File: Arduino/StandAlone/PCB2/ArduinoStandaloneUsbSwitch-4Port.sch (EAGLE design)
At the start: 66 parts, among them U1 INA219AIDCNRSOIC, U2 LM3526M-L, U3 LM3526M-L, U4 ARDUINO_MKRFOX1200PROTOPADS

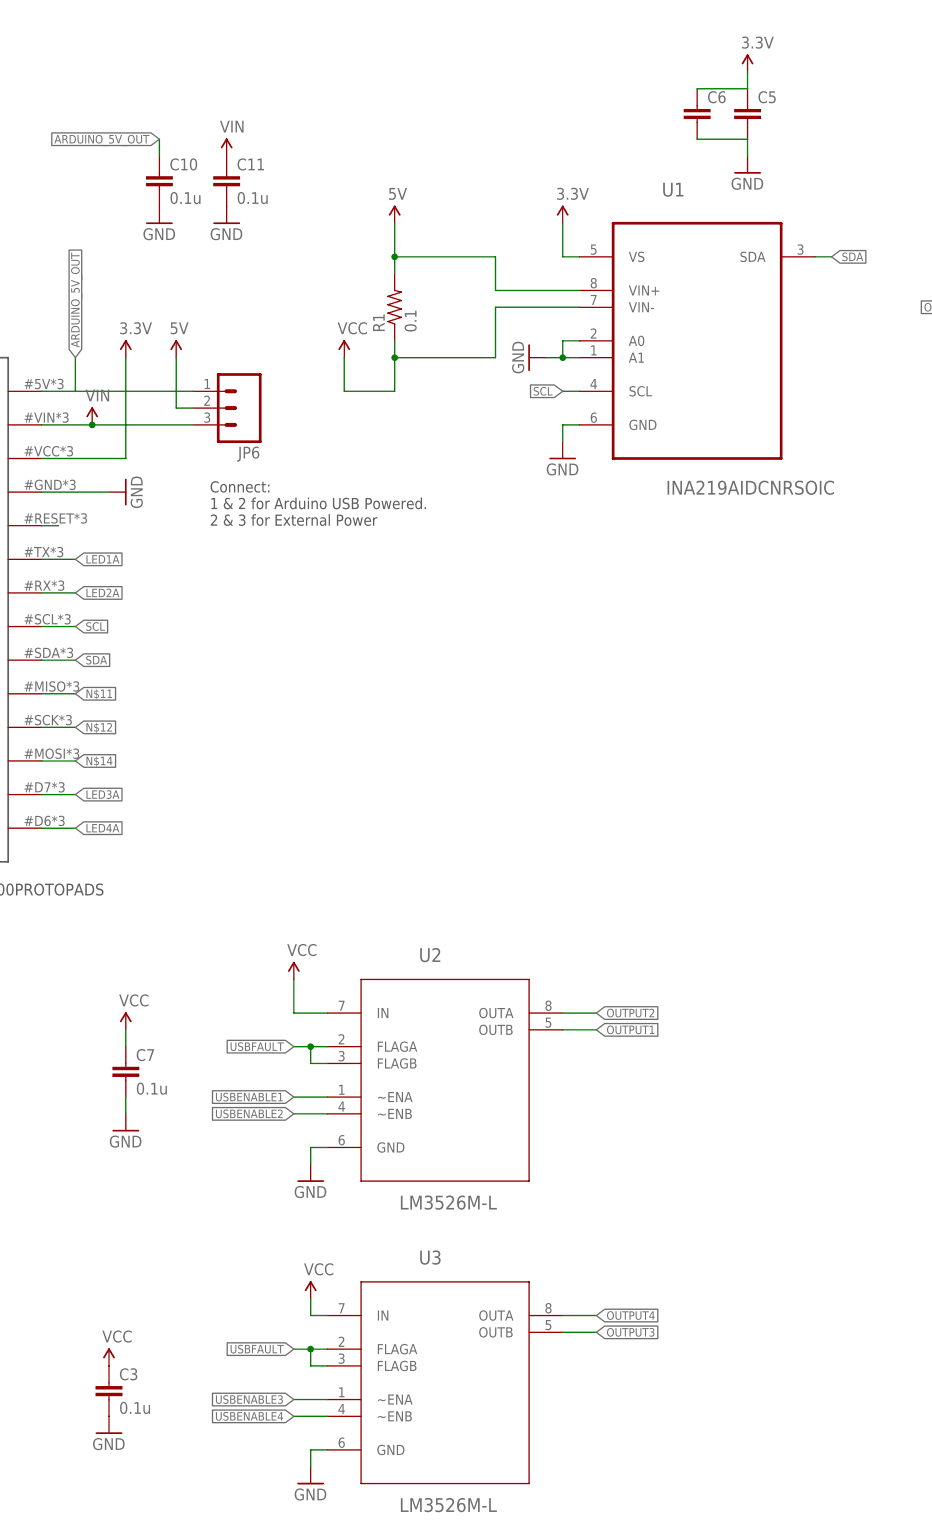
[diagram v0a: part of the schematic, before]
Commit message: Added component values during build.
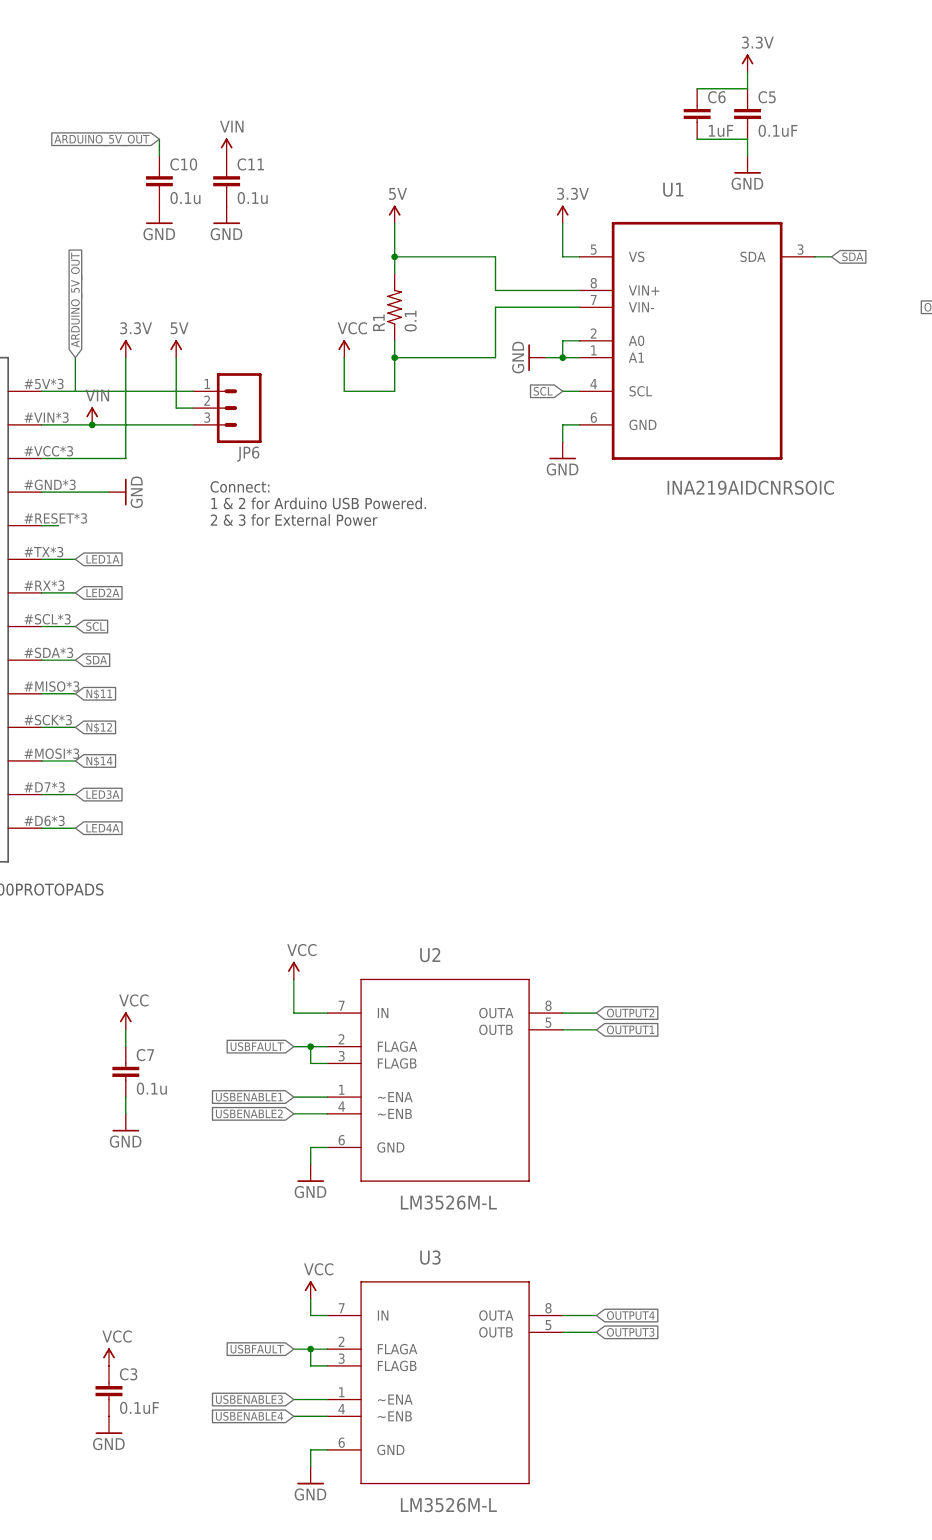
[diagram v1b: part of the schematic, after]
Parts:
- C3: value 0.1u -> 0.1uF
- C5: value (none) -> 0.1uF
- C6: value (none) -> 1uF
- D1: FARNELL (none) -> 1208851
- R1: FARNELL (none) -> 1435952
- S1: FARNELL (none) -> 2533101
- U1: FARNELL (none) -> 2496402
- USB2: FARNELL (none) -> 1177882
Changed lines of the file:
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@@
 </classes>
 <parts>
-<part name="U1" library="INA219AIDCNR" deviceset="INA219AIDCNR" device="SOIC"/>
+<part name="U1" library="INA219AIDCNR" deviceset="INA219AIDCNR" device="SOIC">
+<attribute name="FARNELL" value="2496402"/>
+</part>
 <part name="U4" library="Arduino" deviceset="ARDUINO_MKRFOX1200" device="PROTOPADS"/>
 <part name="FRAME1" library="SparkFun-Aesthetics" deviceset="FRAME-LEDGER" device=""/>
-<part name="R1" library="SparkFun-Resistors" deviceset="0.001OHM-3W-1%(2512)" device="3W/1%" value="0.1"/>
-<part name="USB2" library="Tinamous" deviceset="USB-NEW" device=""/>
+<part name="R1" library="SparkFun-Resistors" deviceset="0.001OHM-3W-1%(2512)" device="3W/1%" value="0.1">
+<attribute name="FARNELL" value="1435952"/>
+</part>
+<part name="USB2" library="Tinamous" deviceset="USB-NEW" device="">
+<attribute name="FARNELL" value="1177882"/>
+</part>
 <part name="USB1" library="Tinamous" deviceset="USB-NEW" device=""/>
 <part name="U2" library="LM3256M-L" deviceset="LM3526M-L" device=""/>
-<part name="S1" library="SparkFun-Electromechanical" deviceset="SWITCH-MOMENTARY-2" device="PTH"/>
+<part name="S1" library="SparkFun-Electromechanical" deviceset="SWITCH-MOMENTARY-2" device="PTH">
+<attribute name="FARNELL" value="2533101"/>
+</part>
 <part name="S2" library="SparkFun-Electromechanical" deviceset="SWITCH-MOMENTARY-2" device="PTH"/>
-<part name="D1" library="SparkFun-LED" deviceset="LED" device="3MM"/>
+<part name="D1" library="SparkFun-LED" deviceset="LED" device="3MM">
+<attribute name="FARNELL" value="1208851"/>
+</part>
 <part name="D2" library="SparkFun-LED" deviceset="LED" device="3MM"/>
 <part name="GND3" library="SparkFun-Aesthetics" deviceset="GND" device=""/>
@@
 <part name="R27" library="SparkFun-Resistors" deviceset="RESISTOR" device="0805-RES" value="100k"/>
 <part name="SUPPLY12" library="SparkFun-Aesthetics" deviceset="3.3V" device=""/>
-<part name="C5" library="SparkFun-Capacitors" deviceset="CAP" device="0805"/>
-<part name="C6" library="SparkFun-Capacitors" deviceset="CAP" device="0805"/>
+<part name="C5" library="SparkFun-Capacitors" deviceset="CAP" device="0805" value="0.1uF"/>
+<part name="C6" library="SparkFun-Capacitors" deviceset="CAP" device="0805" value="1uF"/>
 <part name="SUPPLY14" library="SparkFun-Aesthetics" deviceset="3.3V" device=""/>
 <part name="GND10" library="SparkFun-Aesthetics" deviceset="GND" device=""/>
@@
 <part name="GND8" library="SparkFun-Aesthetics" deviceset="GND" device=""/>
 <part name="GND15" library="SparkFun-Aesthetics" deviceset="GND" device=""/>
-<part name="C3" library="SparkFun-Capacitors" deviceset="CAP" device="0805" value="0.1u"/>
+<part name="C3" library="SparkFun-Capacitors" deviceset="CAP" device="0805" value="0.1uF"/>
 <part name="GND16" library="SparkFun-Aesthetics" deviceset="GND" device=""/>
 <part name="GND19" library="SparkFun-Aesthetics" deviceset="GND" device=""/>
@@
 </plain>
 <instances>
-<instance part="U1" gate="A" x="200.66" y="215.9"/>
+<instance part="U1" gate="A" x="200.66" y="215.9">
+<attribute name="FARNELL" x="200.66" y="215.9" size="1.778" layer="96" display="off"/>
+</instance>
 <instance part="U4" gate="G$1" x="71.12" y="134.62"/>
 <instance part="FRAME1" gate="G$1" x="0" y="0"/>
 <instance part="FRAME1" gate="G$2" x="330.2" y="0"/>
-<instance part="R1" gate="G$1" x="154.94" y="218.44" rot="R90"/>
-<instance part="USB2" gate="G$1" x="299.72" y="193.04"/>
+<instance part="R1" gate="G$1" x="154.94" y="218.44" rot="R90">
+<attribute name="FARNELL" x="154.94" y="218.44" size="1.778" layer="96" rot="R90" display="off"/>
+</instance>
+<instance part="USB2" gate="G$1" x="299.72" y="193.04">
+<attribute name="FARNELL" x="299.72" y="193.04" size="1.778" layer="96" display="off"/>
+</instance>
 <instance part="USB1" gate="G$1" x="383.54" y="195.58"/>
 <instance part="U2" gate="A" x="162.56" y="104.14"/>
-<instance part="S1" gate="G$1" x="302.26" y="182.88"/>
+<instance part="S1" gate="G$1" x="302.26" y="182.88">
+<attribute name="FARNELL" x="302.26" y="182.88" size="1.778" layer="96" display="off"/>
+</instance>
 <instance part="S2" gate="G$1" x="386.08" y="185.42"/>
-<instance part="D1" gate="G$1" x="299.72" y="208.28" rot="R90"/>
+<instance part="D1" gate="G$1" x="299.72" y="208.28" rot="R90">
+<attribute name="FARNELL" x="299.72" y="208.28" size="1.778" layer="96" rot="R90" display="off"/>
+</instance>
 <instance part="D2" gate="G$1" x="383.54" y="210.82" rot="R90"/>
 <instance part="GND3" gate="1" x="393.7" y="180.34"/>

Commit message: Updated device values.
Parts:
- R17, R18, R2, R29, R3, R30, R4, R5, R6, R7, R8, R9: value (none) -> DNP
- U4: value ARDUINO_MKRFOX1200PROTOPADS -> ARDUINO MKR Series
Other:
- note added: "(M3 Machine Screws)"
- note added: "Arduino"
- note added: "Arduino Internal Power Routing: USB -> PFET-> 5V VIN -> PFET-> 5V 5V -> 3v3 reg -> 3V3"
- note added: "Current Monitor"
- note added: "External Power"
- note added: "Mounting Holes"
- note added: "R10/R11 fit with 0R for Ext. USB D+/D- pass-through"
- note added: "Stephen Harrison"
- note added: "USB Ports 1 & 2"
- note added: "USB Ports 1-4 Control"
- note added: "USB Ports 3 & 4"
- note added: "USB Ports Power Monitor"
- note removed: "Arduino Power: USB -> PFET-> 5V VIN -> PFET-> 5V 5V -> 3v3 reg -> 3V3"
- note removed: "USB +/GND reversed!"
- note removed: "possibly d+/d- also"
- moved on the sheet: C1, C10, C11, C2, C4, C5, C6, C8, C9, D1, D2, D3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
